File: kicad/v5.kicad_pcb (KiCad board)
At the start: 2 copper layers, 139 x 78 mm, 108 parts, among them J1 IN1, J2 TP-PRE-FILTER-1, J3 TP-PRE-FILTER-2, J4 Output, J5 Power, J6 Commands, J7 IN2, J8 SHIELD1, J9 SHIELD2, U1 AD8429, U2 AD8429, U3 NE5532, U4 NE5532, U5 ADG442, U6 NE5532, U7 NE5532, U8 TPS7A49, U9 TPS7A30xx

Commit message: Output stage PCB work
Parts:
- J6: value Commands -> CMD
- moved C40 78.0 mm to (152.0, 63.5), turned to 180 degrees
- moved R33 70.5 mm to (160.4, 81.8), turned to 180 degrees
- moved C39 69.8 mm to (145.4, 77.0)
- moved R34 69.7 mm to (166.6, 82.9), turned to 90 degrees
- moved R32 66.4 mm to (157.4, 94.8), turned to 270 degrees
- moved R31 65.1 mm to (153.5, 103.0), turned to 270 degrees
- moved C37 62.4 mm to (145.0, 103.0), turned to 270 degrees
- moved C38 37.7 mm to (172.0, 91.5)
- moved C33 11.9 mm to (186.2, 118.2)
- moved C34 11.9 mm to (186.2, 123.4)
- moved R30 11.9 mm to (173.6, 127.2)
- moved U9 11.9 mm to (179.6, 121.7)
- moved C35 11.9 mm to (170.3, 122.1)
- moved C36 11.9 mm to (167.6, 122.1)
- moved R29 11.9 mm to (173.6, 122.1)
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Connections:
- U5 pad 1: Net-(J6-Pad1) -> Net-(J6-Pad2)
- U5 pad 10: Net-(U3-Pad5) -> Net-(C14-Pad1)
- U5 pad 11: Net-(C8-Pad1) -> Net-(U5-Pad11)
- U5 pad 2: Net-(U5-Pad2) -> Net-(U3-Pad5)
- U5 pad 3: Net-(C14-Pad1) -> Net-(C8-Pad1)
- U5 pad 6: Net-(U5-Pad2) -> Net-(U5-Pad11)
- U5 pad 9: Net-(J6-Pad2) -> Net-(J6-Pad1)
- U6 pad 5: Net-(U5-Pad2) -> Net-(U5-Pad11)
- U8 pad 3: (no net) -> GND
- U8 pad 9: (no net) -> GND
- U9 pad 3: (no net) -> GND
- U9 pad 9: (no net) -> GND
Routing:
- net Net-(C40-Pad1): track 0.00 -> 43.3 mm
- net Net-(C38-Pad2): track 0.00 -> 40.4 mm, vias 0 -> 2
- net Net-(C40-Pad2): track 0.00 -> 28.4 mm
- net Net-(C38-Pad1): track 0.00 -> 26.9 mm
- net Net-(U3-Pad5): track 0.00 -> 25.7 mm, vias 0 -> 2
- net Net-(C39-Pad2): track 17.4 -> 41.8 mm
- net Net-(J4-Pad2): track 23.0 -> 0.00 mm
- net Net-(J4-Pad4): track 21.7 -> 0.00 mm
- net Net-(R28-Pad2): track 18.0 -> 0.00 mm
- net Net-(C37-Pad1): track 0.00 -> 17.4 mm
- net Net-(R27-Pad2): track 14.7 -> 0.00 mm
- net Net-(J6-Pad2): track 0.00 -> 13.3 mm, vias 0 -> 2
- net Net-(R27-Pad1): track 13.1 -> 0.00 mm
- net Net-(C33-Pad1): track 39.7 -> 51.6 mm
- net Net-(U5-Pad11): track 0.00 -> 11.9 mm, vias 0 -> 2
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
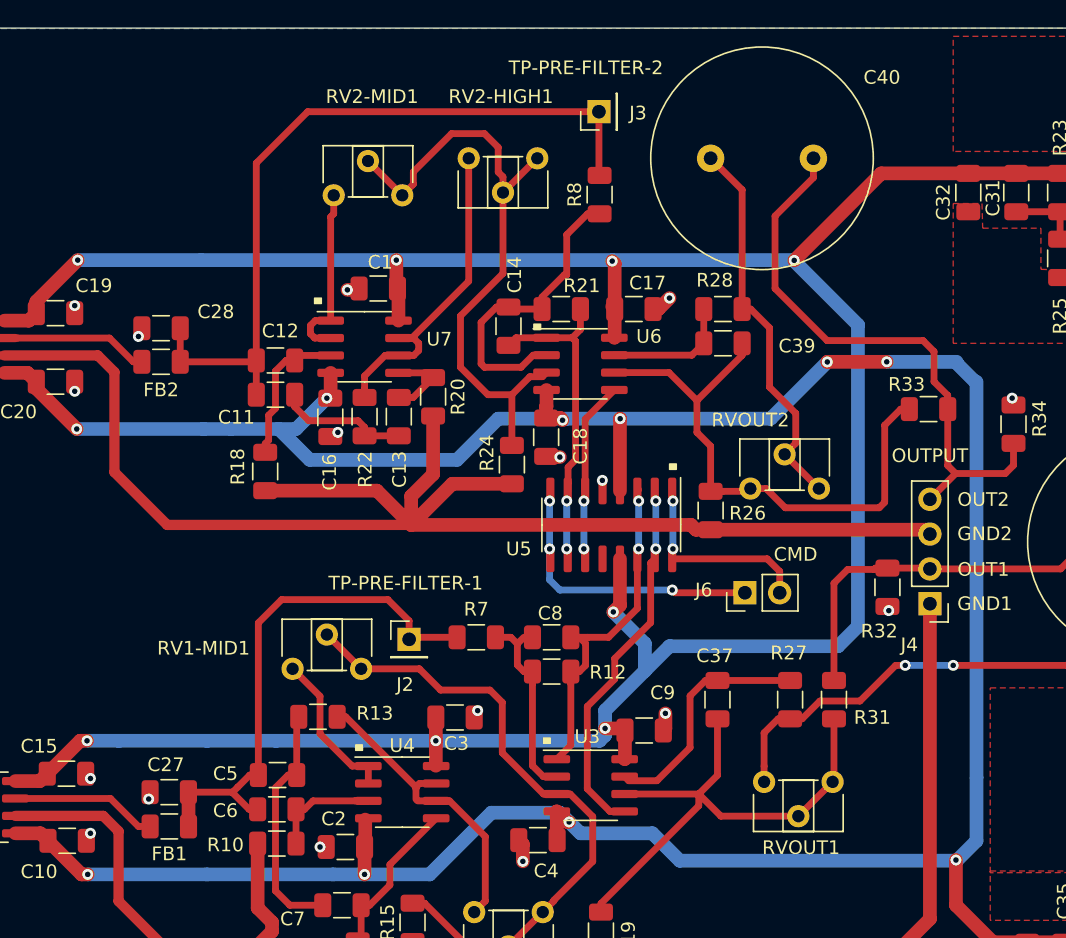
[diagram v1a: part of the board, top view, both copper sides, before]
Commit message: E24 canges on PCB
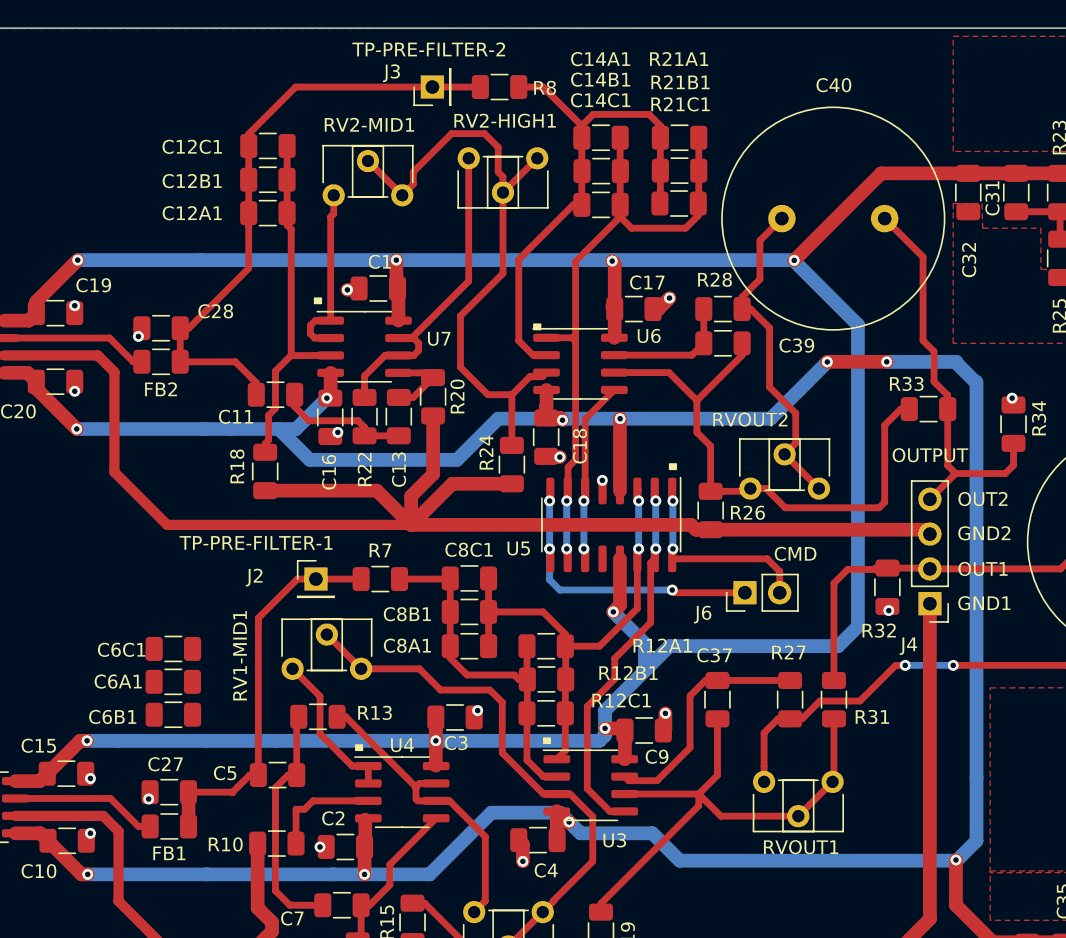
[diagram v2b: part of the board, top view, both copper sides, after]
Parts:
- removed C12: 100n, Capacitor_SMD:C_1206_3216Metric
- removed C14, C8: 160n, Capacitor_SMD:C_1206_3216Metric
- removed R12, R21: 9.92k, Resistor_SMD:R_1206_3216Metric
- added C12A1: 39n, 1%, Capacitor_SMD:C_1206_3216Metric, F.Cu at (112.2, 67.5)
- added C12B1: 39n, 1%, Capacitor_SMD:C_1206_3216Metric, F.Cu at (112.2, 65.1)
- added C12C1: 22n, 1%, Capacitor_SMD:C_1206_3216Metric, F.Cu at (112.2, 62.6)
- added C14A1: 39n, 1%, Capacitor_SMD:C_1206_3216Metric, F.Cu at (136.5, 62.0)
- added C14B1: 39n, 1%, Capacitor_SMD:C_1206_3216Metric, F.Cu at (136.5, 64.4)
- added C14C1: 82n, 1%, Capacitor_SMD:C_1206_3216Metric, F.Cu at (136.5, 66.9)
- added C6A1: 39n, 1%, Capacitor_SMD:C_1206_3216Metric, F.Cu at (105.3, 101.7)
- added C6B1: 39n, 1%, Capacitor_SMD:C_1206_3216Metric, F.Cu at (105.3, 104.1)
- added C8A1: 39n, 1%, Capacitor_SMD:C_1206_3216Metric, F.Cu at (126.9, 99.1)
- added C8B1: 39n, 1%, Capacitor_SMD:C_1206_3216Metric, F.Cu at (126.9, 96.6)
- added C8C1: 82n, 1%, Capacitor_SMD:C_1206_3216Metric, F.Cu at (126.9, 94.2)
- added R12A1: 18k, 1%, Resistor_SMD:R_1206_3216Metric, F.Cu at (132.5, 99.1)
- added R12B1: 39k, 1%, Resistor_SMD:R_1206_3216Metric, F.Cu at (132.5, 101.5)
- added R12C1: 51k, 1%, Resistor_SMD:R_1206_3216Metric, F.Cu at (132.5, 104.0)
- added R21A1: 18k, 1%, Resistor_SMD:R_1206_3216Metric, F.Cu at (142.2, 62.0)
- added R21B1: 39k, 1%, Resistor_SMD:R_1206_3216Metric, F.Cu at (142.2, 66.8)
- added R21C1: 51k, 1%, Resistor_SMD:R_1206_3216Metric, F.Cu at (142.2, 64.4)
- C11, C13: value 6.2n -> 6.8n
- C5, C7: value 6.2n -> 6.8n, 1%
- C6C1: renamed from C6; value 100n -> 22n, 1%
- R10: value 1.5k -> 1.5k, 1%
- R11, R20: value 1.37k -> 1.25k
- R13, R22: value 686 -> 625
- moved C6C1 13.9 mm to (105.3, 99.3)
- moved J3 12.3 mm to (124.2, 58.3)
- moved R8 10.7 mm to (129.1, 58.3), turned to 180 degrees
- moved R7 8.19 mm to (120.4, 94.2)
- moved J2 8.10 mm to (115.7, 94.2)
- moved C40 6.81 mm to (157.2, 67.9)
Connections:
- U8 pad 9: GND -> (no net)
- U9 pad 3: GND -> (no net)
- U9 pad 9: GND -> (no net)
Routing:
- net Net-(C14A1-Pad1): track 22.2 -> 45.2 mm
- net Net-(C14A1-Pad2): track 22.6 -> 38.3 mm
- net Net-(C12A1-Pad1): track 10.9 -> 26.2 mm
- net Net-(C40-Pad1): track 43.3 -> 30.3 mm
- net Net-(C8A1-Pad2): track 15.2 -> 26.8 mm
- net Net-(C11-Pad2): track 56.2 -> 44.6 mm
- net Net-(C27-Pad1): track 38.9 -> 28.7 mm
- net Net-(C8A1-Pad1): track 24.8 -> 34.3 mm
- net Net-(C40-Pad2): track 28.4 -> 24.3 mm

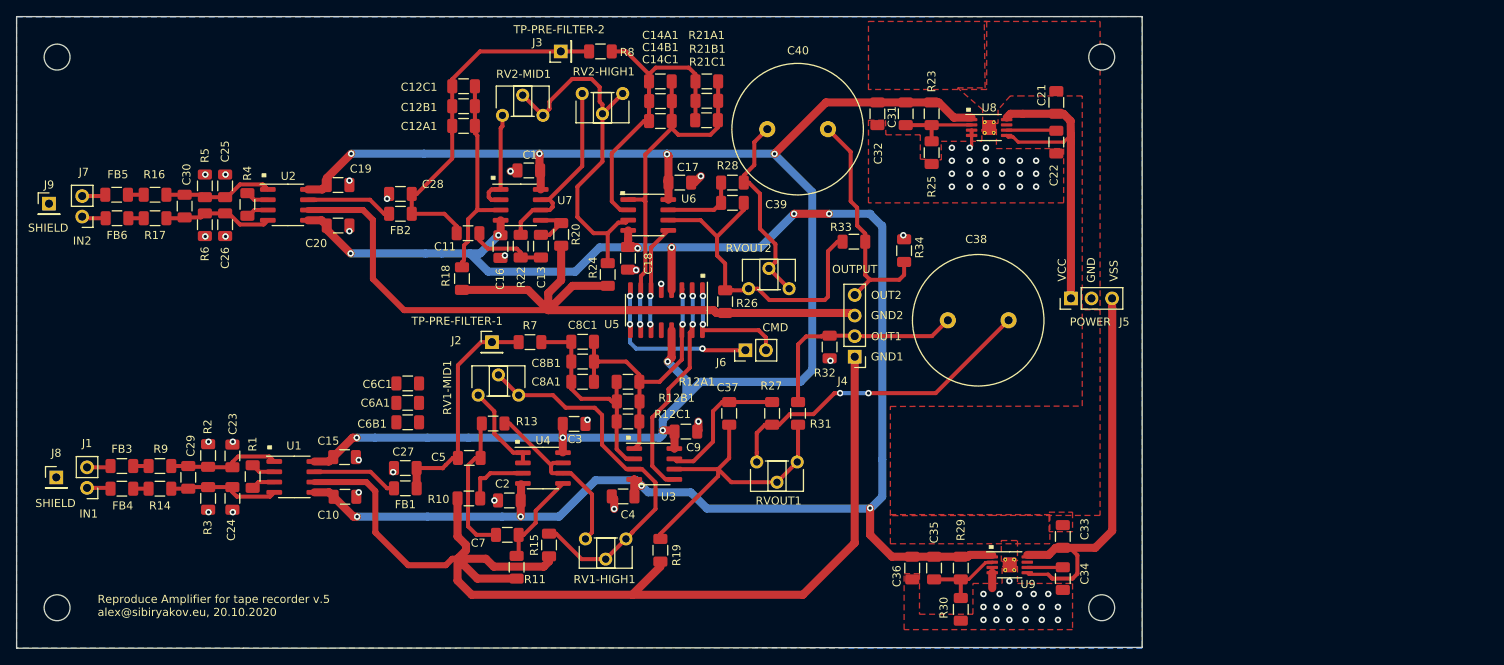
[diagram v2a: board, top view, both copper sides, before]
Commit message: More work on putting filter capacitors, Proper net assignment on power regulators grounds
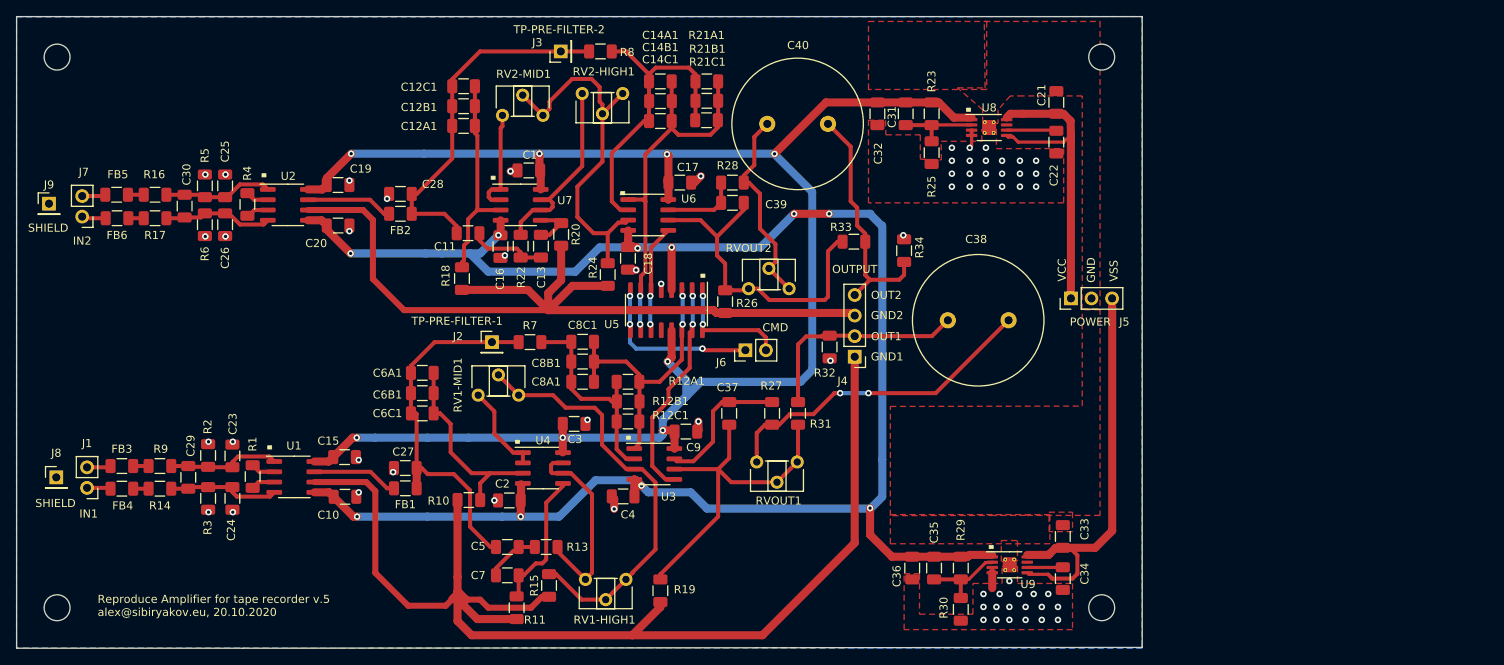
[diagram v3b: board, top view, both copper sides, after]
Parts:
- moved R13 16.6 mm to (122.4, 119.5)
- moved C5 12.0 mm to (117.6, 119.5)
- moved C7 5.00 mm to (117.6, 123.0)
- moved R11 5.00 mm to (118.8, 127.0)
- moved R15 5.00 mm to (122.8, 124.2)
- moved R19 5.00 mm to (136.5, 124.9)
- moved RV1-HIGH1 5.00 mm to (132.2, 123.5)
- moved C6A1 4.12 mm to (107.1, 98.0)
- moved C6C1 4.11 mm to (107.1, 103.0)
- moved C6B1 4.02 mm to (107.1, 100.5)
- moved C40 0.65 mm to (157.2, 67.2)
- moved R10 0.20 mm to (112.8, 113.7)
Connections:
- U8 pad 9: (no net) -> GND
- U9 pad 3: (no net) -> GND
- U9 pad 9: (no net) -> GND
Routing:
- net Net-(C27-Pad1): track 28.7 -> 47.2 mm
- net Net-(C6A1-Pad1): track 8.03 -> 24.8 mm
- net GND: track 255.9 -> 269.1 mm
- net Net-(C5-Pad1): track 17.7 -> 6.82 mm
- net Net-(C7-Pad1): track 11.7 -> 17.2 mm
- net Net-(R15-Pad2): track 47.4 -> 52.4 mm
- net Net-(C37-Pad2): track 39.1 -> 44.1 mm
- net Net-(R13-Pad1): track 22.2 -> 24.8 mm
- net Net-(C40-Pad2): track 24.3 -> 24.9 mm
- net Net-(C40-Pad1): track 30.3 -> 31.0 mm
